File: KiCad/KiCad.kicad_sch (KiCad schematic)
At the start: 28 parts, among them J1 Conn_01x04_Male, J2 Conn_01x04_Male, J3 Conn_01x04_Male, J4 USB_B_Micro, SW1 SW_SPDT, U1 AMS1117-3.3, U2 STM32F103C8T6, Y1 Crystal_GND24

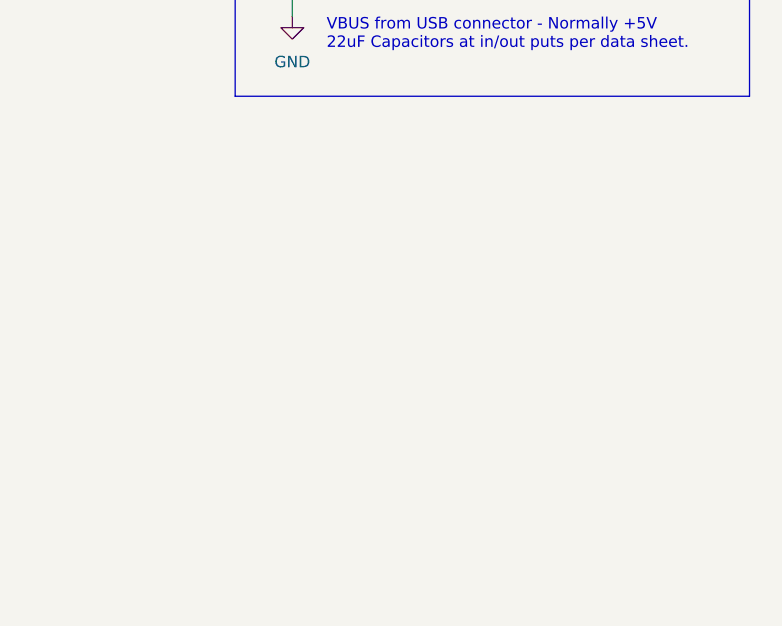
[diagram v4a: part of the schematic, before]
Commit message: Added Mounting holes and arranged board outline
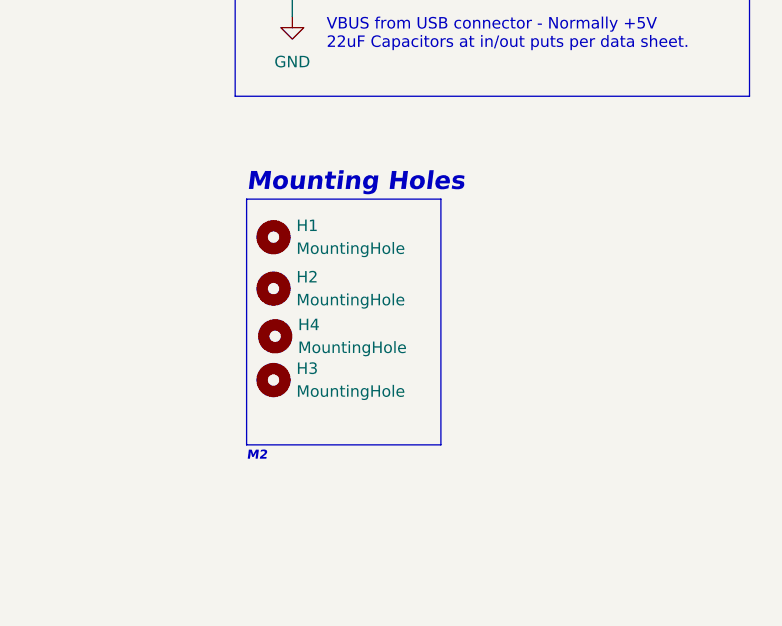
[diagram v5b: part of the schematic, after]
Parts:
- added H1, H2, H3, H4: MountingHole, MountingHole:MountingHole_2.2mm_M2, symbol Mechanical:MountingHole
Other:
- note added: "M2"
- note added: "Mounting Holes"
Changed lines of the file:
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@@
+    (stroke (width 0) (type default) (color 0 0 0 0))
+  )
+  (polyline (pts (xy 40.64 86.36) (xy 40.64 113.665))
     (stroke (width 0) (type default) (color 0 0 0 0))
   )
@@
     (stroke (width 0) (type default) (color 0 0 0 0))
   )
+  (polyline (pts (xy 62.23 86.36) (xy 62.23 113.665))
+    (stroke (width 0) (type default) (color 0 0 0 0))
+  )
+  (polyline (pts (xy 62.23 113.665) (xy 40.64 113.665))
+    (stroke (width 0) (type default) (color 0 0 0 0))
+  )
   (wire (pts (xy 205.74 120.65) (xy 247.65 120.65))
     (stroke (width 0) (type default) (color 0 0 0 0))
@@
   )
   (wire (pts (xy 138.43 81.28) (xy 138.43 87.63))
+    (stroke (width 0) (type default) (color 0 0 0 0))
+  )
+  (polyline (pts (xy 40.64 86.36) (xy 62.23 86.36))
     (stroke (width 0) (type default) (color 0 0 0 0))
   )
@@
   (text "VDDA Pi Filter" (at 212.09 43.18 0)
     (effects (font (size 1.27 1.27)) (justify left bottom))
+  )
+  (text "Mounting Holes" (at 40.64 85.725 0)
+    (effects (font (size 2 2) bold italic) (justify left bottom))
   )
   (text "VBUS from USB connector - Normally +5V\n22uF Capacitors at in/out puts per data sheet."
@@
     (effects (font (size 1.27 1.27)) (justify left bottom))
   )
+  (text "M2\n" (at 40.64 115.57 0)
+    (effects (font (size 1 1) bold italic) (justify left bottom))
+  )
   (text "Basic STM32\n" (at 15.24 20.32 0)
     (effects (font (size 3 3) bold italic) (justify left bottom))
@@
     (pin "1")
   )
+  (symbol (lib_id "Mechanical:MountingHole") (at 43.6336 106.463 0) (unit 1)
+    (in_bom yes) (on_board yes)
+    (property "Reference" "H3" (id 0) (at 46.1736 105.1929 0)
+      (effects (font (size 1.27 1.27)) (justify left))
+    )
+    (property "Value" "MountingHole" (id 1) (at 46.1736 107.7329 0)
+      (effects (font (size 1.27 1.27)) (justify left))
+    )
+    (property "Footprint" "MountingHole:MountingHole_2.2mm_M2" (id 2) (at 43.6336 98.208 0)
+      (effects (font (size 1.27 1.27)) hide)
+    )
+    (property "Datasheet" "~" (id 3) (at 43.6336 106.463 0)
+      (effects (font (size 1.27 1.27)) hide)
+    )
+  )
   (symbol (lib_id "Device:R") (at 163.83 69.85 90) (unit 1)
     (in_bom yes) (on_board yes)
@@
     (pin "1")
     (pin "2")
+  )
+  (symbol (lib_id "Mechanical:MountingHole") (at 43.6336 90.588 0) (unit 1)
+    (in_bom yes) (on_board yes)
+    (property "Reference" "H1" (id 0) (at 46.1736 89.3179 0)
+      (effects (font (size 1.27 1.27)) (justify left))
+    )
+    (property "Value" "MountingHole" (id 1) (at 46.1736 91.8579 0)
+      (effects (font (size 1.27 1.27)) (justify left))
+    )
+    (property "Footprint" "MountingHole:MountingHole_2.2mm_M2" (id 2) (at 43.6336 82.333 0)
+      (effects (font (size 1.27 1.27)) hide)
+    )
+    (property "Datasheet" "~" (id 3) (at 43.6336 90.588 0)
+      (effects (font (size 1.27 1.27)) hide)
+    )
   )
   (symbol (lib_id "power:GND") (at 241.3 57.15 0) (unit 1)
@@
     (pin "1")
   )
+  (symbol (lib_id "Mechanical:MountingHole") (at 43.6336 96.303 0) (unit 1)
+    (in_bom yes) (on_board yes)
+    (property "Reference" "H2" (id 0) (at 46.1736 95.0329 0)
+      (effects (font (size 1.27 1.27)) (justify left))
+    )
+    (property "Value" "MountingHole" (id 1) (at 46.1736 97.5729 0)
+      (effects (font (size 1.27 1.27)) (justify left))
+    )
+    (property "Footprint" "MountingHole:MountingHole_2.2mm_M2" (id 2) (at 43.6336 88.048 0)
+      (effects (font (size 1.27 1.27)) hide)
+    )
+    (property "Datasheet" "~" (id 3) (at 43.6336 96.303 0)
+      (effects (font (size 1.27 1.27)) hide)
+    )
+  )
   (symbol (lib_id "Connector:Conn_01x04_Male") (at 143.51 107.95 0) (unit 1)
     (in_bom yes) (on_board yes)
@@
     (pin "1")
   )
+  (symbol (lib_id "Mechanical:MountingHole") (at 43.815 101.6 0) (unit 1)
+    (in_bom yes) (on_board yes)
+    (property "Reference" "H4" (id 0) (at 46.355 100.3299 0)
+      (effects (font (size 1.27 1.27)) (justify left))
+    )
+    (property "Value" "MountingHole" (id 1) (at 46.355 102.8699 0)
+      (effects (font (size 1.27 1.27)) (justify left))
+    )
+    (property "Footprint" "MountingHole:MountingHole_2.2mm_M2" (id 2) (at 43.815 93.345 0)
+      (effects (font (size 1.27 1.27)) hide)
+    )
+    (property "Datasheet" "~" (id 3) (at 43.815 101.6 0)
+      (effects (font (size 1.27 1.27)) hide)
+    )
+  )
   (symbol (lib_id "Device:C") (at 151.13 53.34 0) (unit 1)
     (in_bom yes) (on_board yes) (fields_autoplaced)
@@
       (reference "FB1") (unit 1) (value "120R") (footprint "Inductor_SMD:L_0603_1608Metric")
     )
+    (path "/9f5f60c4-0edc-4136-aec5-b49fa49db8ad"
+      (reference "H1") (unit 1) (value "MountingHole") (footprint "MountingHole:MountingHole_2.2mm_M2")
+    )
+    (path "/cb82370a-778c-4b55-a358-3342319f2c82"
+      (reference "H2") (unit 1) (value "MountingHole") (footprint "MountingHole:MountingHole_2.2mm_M2")
+    )
+    (path "/27468ac5-d74a-4694-8ea6-29e439a7adc4"
+      (reference "H3") (unit 1) (value "MountingHole") (footprint "MountingHole:MountingHole_2.2mm_M2")
+    )
+    (path "/ed605e93-6dfa-400b-acb2-534dc3722aed"
+      (reference "H4") (unit 1) (value "MountingHole") (footprint "MountingHole:MountingHole_2.2mm_M2")
+    )
     (path "/cbbb60b7-1e6b-4a50-b1c6-77d3a0e11f02"

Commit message: Sourced parts & Changed some components
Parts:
- J4: footprint Connector_USB:USB_Micro-B_Wuerth_629105150521 -> Connector_USB:USB_Micro-B_Molex_47346-0001
- Y1: footprint Crystal:Crystal_SMD_3225-4Pin_3.2x2.5mm_HandSoldering -> Crystal:Crystal_SMD_3225-4Pin_3.2x2.5mm
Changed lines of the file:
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@@
       (effects (font (size 0.95 0.95)))
     )
-    (property "Footprint" "Crystal:Crystal_SMD_3225-4Pin_3.2x2.5mm_HandSoldering" (id 2) (at 149.86 87.63 0)
+    (property "Footprint" "Crystal:Crystal_SMD_3225-4Pin_3.2x2.5mm" (id 2) (at 149.86 87.63 0)
       (effects (font (size 1.27 1.27)) hide)
     )
@@
       (effects (font (size 1.27 1.27)) (justify right))
     )
-    (property "Footprint" "Connector_USB:USB_Micro-B_Wuerth_629105150521" (id 2) (at 251.46 121.92 0)
+    (property "Footprint" "Connector_USB:USB_Micro-B_Molex_47346-0001" (id 2) (at 251.46 121.92 0)
       (effects (font (size 1.27 1.27)) hide)
     )
@@
     )
     (path "/b55665fe-b444-4d21-a878-c93dca59d36e"
-      (reference "J4") (unit 1) (value "USB_B_Micro") (footprint "Connector_USB:USB_Micro-B_Wuerth_629105150521")
+      (reference "J4") (unit 1) (value "USB_B_Micro") (footprint "Connector_USB:USB_Micro-B_Molex_47346-0001")
     )
     (path "/5f189379-a320-4c71-aff3-b9355e904778"
@@
     )
     (path "/84f018b8-303a-40ec-9b42-114981faf0a7"
-      (reference "Y1") (unit 1) (value "Crystal_GND24") (footprint "Crystal:Crystal_SMD_3225-4Pin_3.2x2.5mm_HandSoldering")
-    )
-  )
+      (reference "Y1") (unit 1) (value "Crystal_GND24") (footprint "Crystal:Crystal_SMD_3225-4Pin_3.2x2.5mm")
+    )
+  )
